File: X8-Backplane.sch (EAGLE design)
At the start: 17 parts, among them U1 BD6221FSOP, U2 MIC29501-5.0WU, U3 MIC29501-5.0WU, U4 FQB27P06, U5 FQB27P06

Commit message: Added a mosfet for an led for the blue tooth
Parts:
- added U6: FQB27P06, CamSensComponents:FQB27P06
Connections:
- new net BT_LED_5V: U$4G$1.15, U$4G$1.16, U6.D2
- new net BT_LED_ON: PCB1.GPIO16, U6.G2
- net +5V_CAMERA_TUBE: now also U6.S2
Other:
- note added: "BLUE TOOTH LED"

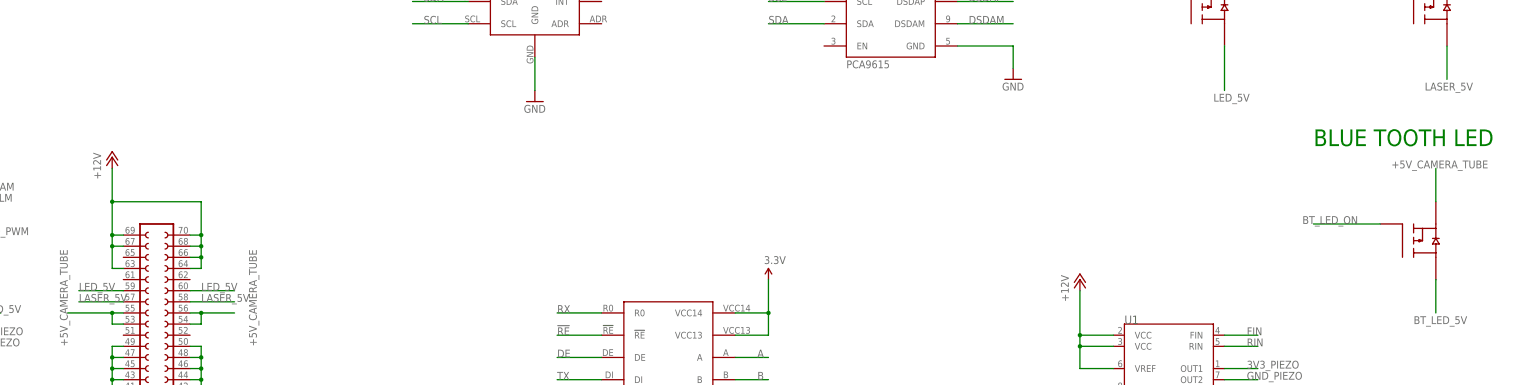
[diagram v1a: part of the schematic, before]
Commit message: Started initial routing on the board
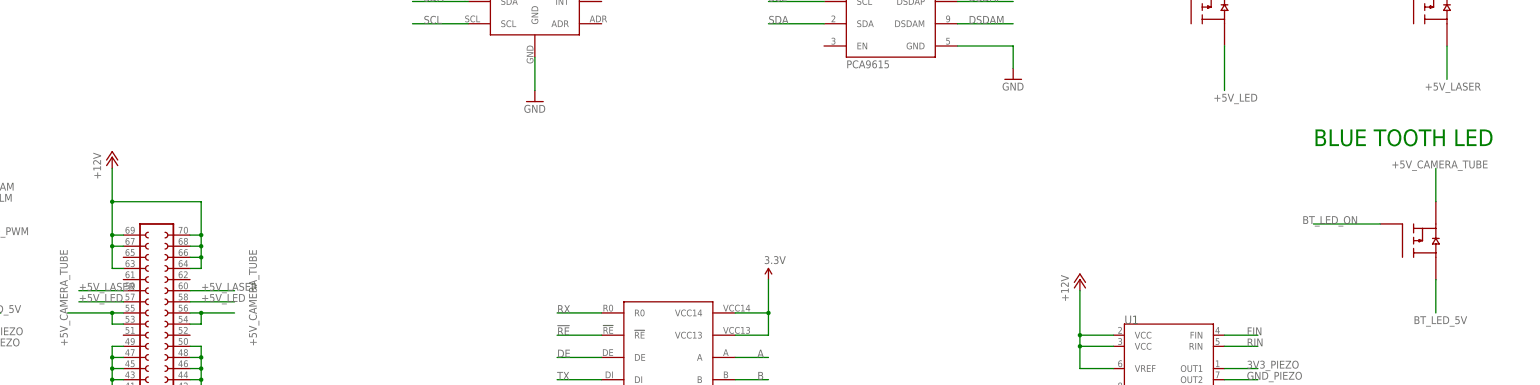
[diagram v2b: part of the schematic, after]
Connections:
- removed net LASER_5V: U$4G$2.17, U$4G$2.18, U5.D2
- removed net LED_5V: U$4G$2.19, U$4G$2.20, U4.D2
- new net +5V_LASER: U$4G$2.19, U$4G$2.20, U5.D2
- new net +5V_LED: U$4G$2.17, U$4G$2.18, U4.D2
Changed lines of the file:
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@@
 <grid distance="0.1" unitdist="inch" unit="inch" style="lines" multiple="1" display="no" altdistance="0.01" altunitdist="inch" altunit="inch"/>
 <layers>
-<layer number="1" name="Top" color="4" fill="1" visible="yes" active="no"/>
-<layer number="2" name="Route2" color="1" fill="3" visible="yes" active="no"/>
-<layer number="3" name="Route3" color="4" fill="3" visible="yes" active="no"/>
-<layer number="4" name="Route4" color="1" fill="4" visible="yes" active="no"/>
-<layer number="5" name="Route5" color="4" fill="4" visible="yes" active="no"/>
-<layer number="6" name="Route6" color="1" fill="8" visible="yes" active="no"/>
-<layer number="7" name="Route7" color="4" fill="8" visible="yes" active="no"/>
-<layer number="8" name="Route8" color="1" fill="2" visible="yes" active="no"/>
-<layer number="9" name="Route9" color="4" fill="2" visible="yes" active="no"/>
-<layer number="10" name="Route10" color="1" fill="7" visible="yes" active="no"/>
-<layer number="11" name="Route11" color="4" fill="7" visible="yes" active="no"/>
-<layer number="12" name="Route12" color="1" fill="5" visible="yes" active="no"/>
-<layer number="13" name="Route13" color="4" fill="5" visible="yes" active="no"/>
-<layer number="14" name="Route14" color="1" fill="6" visible="yes" active="no"/>
-<layer number="15" name="Route15" color="4" fill="6" visible="yes" active="no"/>
-<layer number="16" name="Bottom" color="1" fill="1" visible="yes" active="no"/>
-<layer number="17" name="Pads" color="2" fill="1" visible="yes" active="no"/>
-<layer number="18" name="Vias" color="2" fill="1" visible="yes" active="no"/>
-<layer number="19" name="Unrouted" color="6" fill="1" visible="yes" active="no"/>
-<layer number="20" name="Dimension" color="15" fill="1" visible="yes" active="no"/>
-<layer number="21" name="tPlace" color="7" fill="1" visible="yes" active="no"/>
-<layer number="22" name="bPlace" color="7" fill="1" visible="yes" active="no"/>
-<layer number="23" name="tOrigins" color="15" fill="1" visible="yes" active="no"/>
-<layer number="24" name="bOrigins" color="15" fill="1" visible="yes" active="no"/>
-<layer number="25" name="tNames" color="7" fill="1" visible="yes" active="no"/>
-<layer number="26" name="bNames" color="7" fill="1" visible="yes" active="no"/>
-<layer number="27" name="tValues" color="7" fill="1" visible="yes" active="no"/>
-<layer number="28" name="bValues" color="7" fill="1" visible="yes" active="no"/>
+<layer number="1" name="Top" color="4" fill="1" visible="no" active="no"/>
+<layer number="2" name="Route2" color="1" fill="3" visible="no" active="no"/>
+<layer number="3" name="Route3" color="4" fill="3" visible="no" active="no"/>
+<layer number="4" name="Route4" color="1" fill="4" visible="no" active="no"/>
+<layer number="5" name="Route5" color="4" fill="4" visible="no" active="no"/>
+<layer number="6" name="Route6" color="1" fill="8" visible="no" active="no"/>
+<layer number="7" name="Route7" color="4" fill="8" visible="no" active="no"/>
+<layer number="8" name="Route8" color="1" fill="2" visible="no" active="no"/>
+<layer number="9" name="Route9" color="4" fill="2" visible="no" active="no"/>
+<layer number="10" name="Route10" color="1" fill="7" visible="no" active="no"/>
+<layer number="11" name="Route11" color="4" fill="7" visible="no" active="no"/>
+<layer number="12" name="Route12" color="1" fill="5" visible="no" active="no"/>
+<layer number="13" name="Route13" color="4" fill="5" visible="no" active="no"/>
+<layer number="14" name="Route14" color="1" fill="6" visible="no" active="no"/>
+<layer number="15" name="Route15" color="4" fill="6" visible="no" active="no"/>
+<layer number="16" name="Bottom" color="1" fill="1" visible="no" active="no"/>
+<layer number="17" name="Pads" color="2" fill="1" visible="no" active="no"/>
+<layer number="18" name="Vias" color="2" fill="1" visible="no" active="no"/>
+<layer number="19" name="Unrouted" color="6" fill="1" visible="no" active="no"/>
+<layer number="20" name="Dimension" color="15" fill="1" visible="no" active="no"/>
+<layer number="21" name="tPlace" color="7" fill="1" visible="no" active="no"/>
+<layer number="22" name="bPlace" color="7" fill="1" visible="no" active="no"/>
+<layer number="23" name="tOrigins" color="15" fill="1" visible="no" active="no"/>
+<layer number="24" name="bOrigins" color="15" fill="1" visible="no" active="no"/>
+<layer number="25" name="tNames" color="7" fill="1" visible="no" active="no"/>
+<layer number="26" name="bNames" color="7" fill="1" visible="no" active="no"/>
+<layer number="27" name="tValues" color="7" fill="1" visible="no" active="no"/>
+<layer number="28" name="bValues" color="7" fill="1" visible="no" active="no"/>
 <layer number="29" name="tStop" color="7" fill="3" visible="no" active="no"/>
 <layer number="30" name="bStop" color="7" fill="6" visible="no" active="no"/>
@@
 <layer number="35" name="tGlue" color="7" fill="4" visible="no" active="no"/>
 <layer number="36" name="bGlue" color="7" fill="5" visible="no" active="no"/>
-<layer number="37" name="tTest" color="7" fill="1" visible="yes" active="no"/>
-<layer number="38" name="bTest" color="7" fill="1" visible="yes" active="no"/>
+<layer number="37" name="tTest" color="7" fill="1" visible="no" active="no"/>
+<layer number="38" name="bTest" color="7" fill="1" visible="no" active="no"/>
 <layer number="39" name="tKeepout" color="4" fill="11" visible="no" active="no"/>
 <layer number="40" name="bKeepout" color="1" fill="11" visible="no" active="no"/>
@@
 <layer number="44" name="Drills" color="7" fill="1" visible="no" active="no"/>
 <layer number="45" name="Holes" color="7" fill="1" visible="no" active="no"/>
-<layer number="46" name="Milling" color="3" fill="1" visible="yes" active="no"/>
-<layer number="47" name="Measures" color="7" fill="1" visible="yes" active="no"/>
-<layer number="48" name="Document" color="7" fill="1" visible="yes" active="no"/>
-<layer number="49" name="Reference" color="7" fill="1" visible="yes" active="no"/>
-<layer number="50" name="dxf" color="7" fill="1" visible="yes" active="no"/>
-<layer number="51" name="tDocu" color="7" fill="1" visible="yes" active="no"/>
-<layer number="52" name="bDocu" color="7" fill="1" visible="yes" active="no"/>
-<layer number="53" name="tGND_GNDA" color="7" fill="1" visible="yes" active="no"/>
-<layer number="54" name="bGND_GNDA" color="7" fill="1" visible="yes" active="no"/>
-<layer number="56" name="wert" color="7" fill="1" visible="yes" active="no"/>
-<layer number="57" name="tCAD" color="7" fill="1" visible="yes" active="no"/>
-<layer number="59" name="tCarbon" color="7" fill="1" visible="yes" active="no"/>
-<layer number="60" name="bCarbon" color="7" fill="1" visible="yes" active="no"/>
+<layer number="46" name="Milling" color="3" fill="1" visible="no" active="no"/>
+<layer number="47" name="Measures" color="7" fill="1" visible="no" active="no"/>
+<layer number="48" name="Document" color="7" fill="1" visible="no" active="no"/>
+<layer number="49" name="Reference" color="7" fill="1" visible="no" active="no"/>
+<layer number="50" name="dxf" color="7" fill="1" visible="no" active="no"/>
+<layer number="51" name="tDocu" color="7" fill="1" visible="no" active="no"/>
+<layer number="52" name="bDocu" color="7" fill="1" visible="no" active="no"/>
+<layer number="53" name="tGND_GNDA" color="7" fill="1" visible="no" active="no"/>
+<layer number="54" name="bGND_GNDA" color="7" fill="1" visible="no" active="no"/>
+<layer number="56" name="wert" color="7" fill="1" visible="no" active="no"/>
+<layer number="57" name="tCAD" color="7" fill="1" visible="no" active="no"/>
+<layer number="59" name="tCarbon" color="7" fill="1" visible="no" active="no"/>
+<layer number="60" name="bCarbon" color="7" fill="1" visible="no" active="no"/>
 <layer number="90" name="Modules" color="5" fill="1" visible="yes" active="yes"/>
 <layer number="91" name="Nets" color="2" fill="1" visible="yes" active="yes"/>
@@
 </segment>
 </net>
-<net name="LED_5V" class="0">
+<net name="+5V_LED" class="0">
 <segment>
 <pinref part="U4" gate="G$1" pin="D2"/>
@@
 </segment>
 <segment>
+<pinref part="U$4" gate="G$2" pin="18"/>
+<wire x1="251.46" y1="101.6" x2="261.62" y2="101.6" width="0.1524" layer="91"/>
+<label x="254" y="101.6" size="1.778" layer="95"/>
+</segment>
+<segment>
+<pinref part="U$4" gate="G$2" pin="17"/>
+<wire x1="236.22" y1="101.6" x2="226.06" y2="101.6" width="0.1524" layer="91"/>
+<label x="226.06" y="101.6" size="1.778" layer="95"/>
+</segment>
+</net>
+<net name="+5V_LASER" class="0">
+<segment>
+<pinref part="U5" gate="G$1" pin="D2"/>
+<wire x1="538.48" y1="160.02" x2="538.48" y2="152.4" width="0.1524" layer="91"/>
+<label x="533.4" y="149.86" size="1.778" layer="95"/>
+</segment>
+<segment>
+<pinref part="U$4" gate="G$2" pin="20"/>
+<wire x1="251.46" y1="104.14" x2="261.62" y2="104.14" width="0.1524" layer="91"/>
+<label x="254" y="104.14" size="1.778" layer="95"/>
+</segment>
+<segment>
 <pinref part="U$4" gate="G$2" pin="19"/>
 <wire x1="236.22" y1="104.14" x2="226.06" y2="104.14" width="0.1524" layer="91"/>
 <label x="226.06" y="104.14" size="1.778" layer="95"/>
 </segment>
-<segment>
-<pinref part="U$4" gate="G$2" pin="20"/>
-<wire x1="251.46" y1="104.14" x2="261.62" y2="104.14" width="0.1524" layer="91"/>
-<label x="254" y="104.14" size="1.778" layer="95"/>
-</segment>
-</net>
-<net name="LASER_5V" class="0">
-<segment>
-<pinref part="U5" gate="G$1" pin="D2"/>
-<wire x1="538.48" y1="160.02" x2="538.48" y2="152.4" width="0.1524" layer="91"/>
-<label x="533.4" y="149.86" size="1.778" layer="95"/>
-</segment>
-<segment>
-<pinref part="U$4" gate="G$2" pin="17"/>
-<wire x1="236.22" y1="101.6" x2="226.06" y2="101.6" width="0.1524" layer="91"/>
-<label x="226.06" y="101.6" size="1.778" layer="95"/>
-</segment>
-<segment>
-<pinref part="U$4" gate="G$2" pin="18"/>
-<wire x1="251.46" y1="101.6" x2="261.62" y2="101.6" width="0.1524" layer="91"/>
-<label x="254" y="101.6" size="1.778" layer="95"/>
-</segment>
-</net>
+</net>

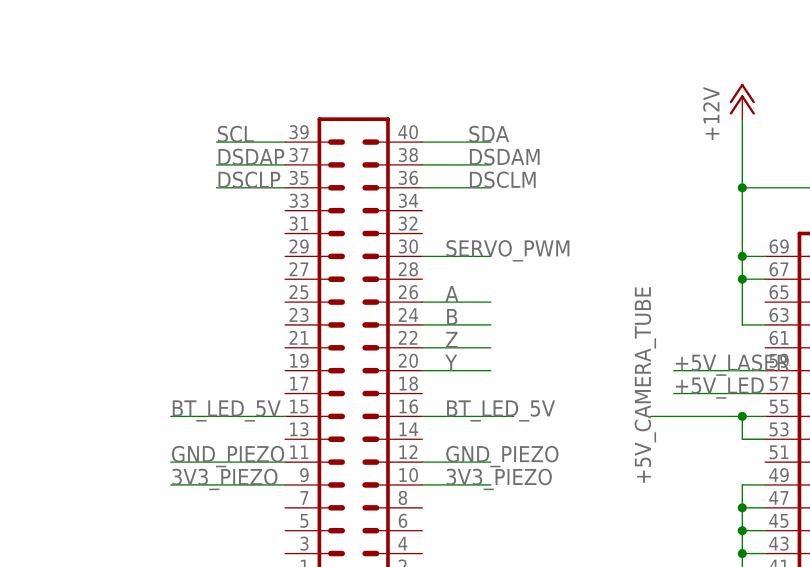
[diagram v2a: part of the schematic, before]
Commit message: Redid routing and moved components
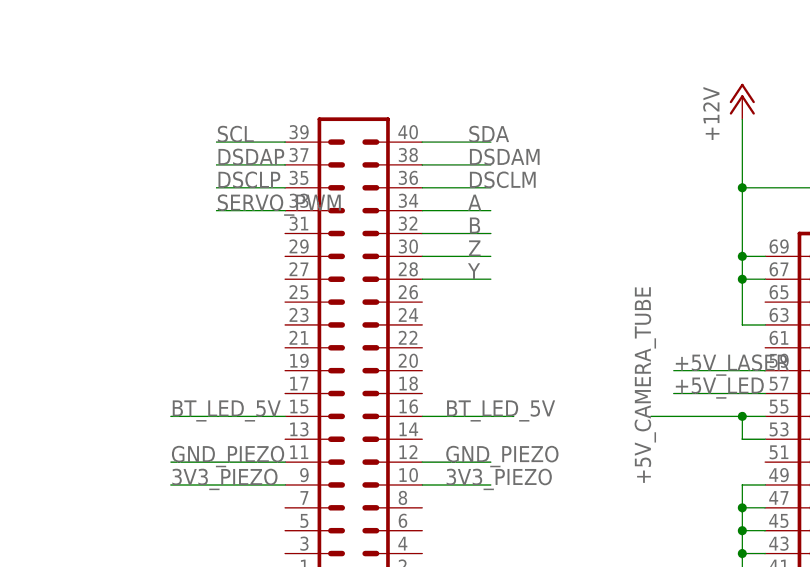
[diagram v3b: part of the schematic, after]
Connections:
- net A: now also U$4G$1.33; no longer U$4G$1.25
- net B: now also U$4G$1.31; no longer U$4G$1.23
- net SERVO_PWM: now also U$4G$1.34; no longer U$4G$1.29
- net Y: now also U$4G$1.27; no longer U$4G$1.19
- net Z: now also U$4G$1.29; no longer U$4G$1.21
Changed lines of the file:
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@@
 </segment>
 <segment>
-<pinref part="U$4" gate="G$1" pin="25"/>
-<wire x1="198.12" y1="111.76" x2="205.74" y2="111.76" width="0.1524" layer="91"/>
-<label x="200.66" y="111.76" size="1.778" layer="95"/>
+<pinref part="U$4" gate="G$1" pin="33"/>
+<wire x1="198.12" y1="121.92" x2="205.74" y2="121.92" width="0.1524" layer="91"/>
+<label x="203.2" y="121.92" size="1.778" layer="95"/>
 </segment>
 </net>
@@
 </segment>
 <segment>
-<pinref part="U$4" gate="G$1" pin="23"/>
-<wire x1="198.12" y1="109.22" x2="205.74" y2="109.22" width="0.1524" layer="91"/>
-<label x="200.66" y="109.22" size="1.778" layer="95"/>
+<pinref part="U$4" gate="G$1" pin="31"/>
+<wire x1="198.12" y1="119.38" x2="205.74" y2="119.38" width="0.1524" layer="91"/>
+<label x="203.2" y="119.38" size="1.778" layer="95"/>
 </segment>
 </net>
@@
 </segment>
 <segment>
-<pinref part="U$4" gate="G$1" pin="21"/>
-<wire x1="198.12" y1="106.68" x2="205.74" y2="106.68" width="0.1524" layer="91"/>
-<label x="200.66" y="106.68" size="1.778" layer="95"/>
+<pinref part="U$4" gate="G$1" pin="29"/>
+<wire x1="198.12" y1="116.84" x2="205.74" y2="116.84" width="0.1524" layer="91"/>
+<label x="203.2" y="116.84" size="1.778" layer="95"/>
 </segment>
 </net>
@@
 </segment>
 <segment>
-<pinref part="U$4" gate="G$1" pin="19"/>
-<wire x1="198.12" y1="104.14" x2="205.74" y2="104.14" width="0.1524" layer="91"/>
-<label x="200.66" y="104.14" size="1.778" layer="95"/>
+<pinref part="U$4" gate="G$1" pin="27"/>
+<wire x1="198.12" y1="114.3" x2="205.74" y2="114.3" width="0.1524" layer="91"/>
+<label x="203.2" y="114.3" size="1.778" layer="95"/>
 </segment>
 </net>
@@
 <net name="SERVO_PWM" class="0">
 <segment>
-<pinref part="U$4" gate="G$1" pin="29"/>
-<wire x1="198.12" y1="116.84" x2="205.74" y2="116.84" width="0.1524" layer="91"/>
-<label x="200.66" y="116.84" size="1.778" layer="95"/>
-</segment>
-<segment>
 <pinref part="PCB1" gate="G$1" pin="GPIO18"/>
 <wire x1="40.64" y1="68.58" x2="20.32" y2="68.58" width="0.1524" layer="91"/>
 <label x="20.32" y="68.58" size="1.778" layer="95"/>
 </segment>
+<segment>
+<pinref part="U$4" gate="G$1" pin="34"/>
+<wire x1="182.88" y1="121.92" x2="175.26" y2="121.92" width="0.1524" layer="91"/>
+<label x="175.26" y="121.92" size="1.778" layer="95"/>
+</segment>
 </net>
